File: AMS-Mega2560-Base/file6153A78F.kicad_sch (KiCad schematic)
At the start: 18 parts, among them Q17 BS250, Q21 LTV-847

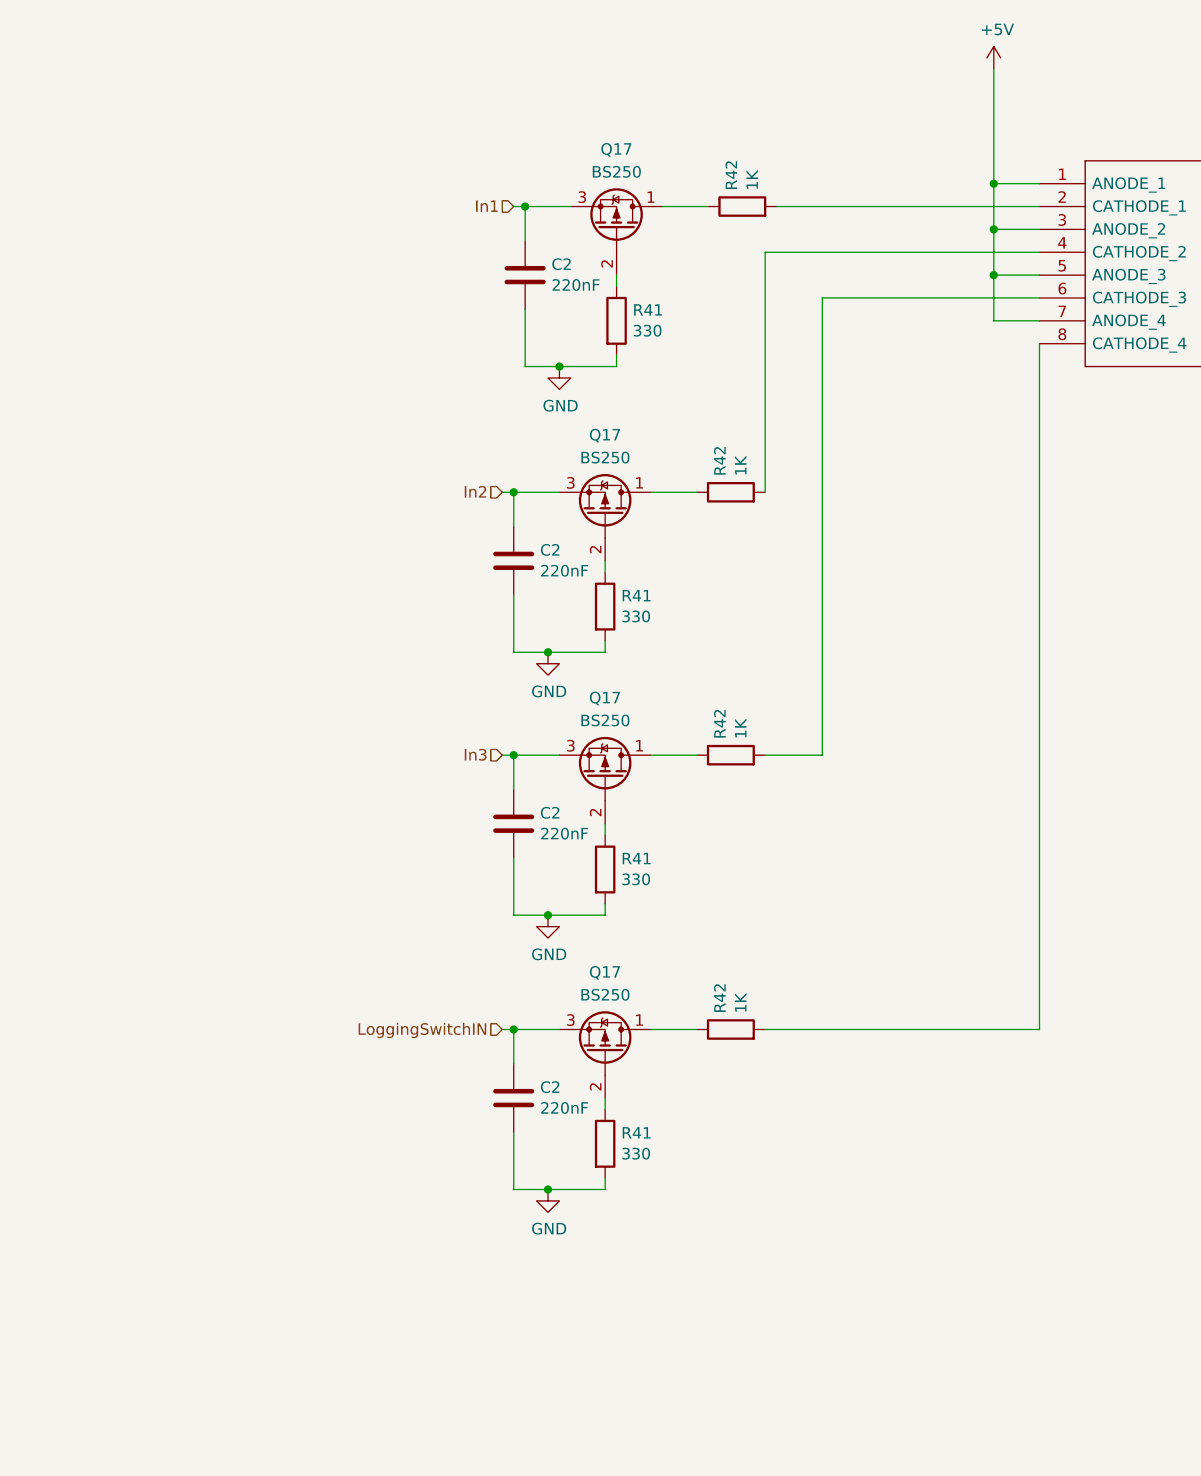
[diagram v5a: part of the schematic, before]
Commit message: * got parts placed * modified the Input circuit design to include Nchannel fet Needs the tricky routes done before doing autoroute
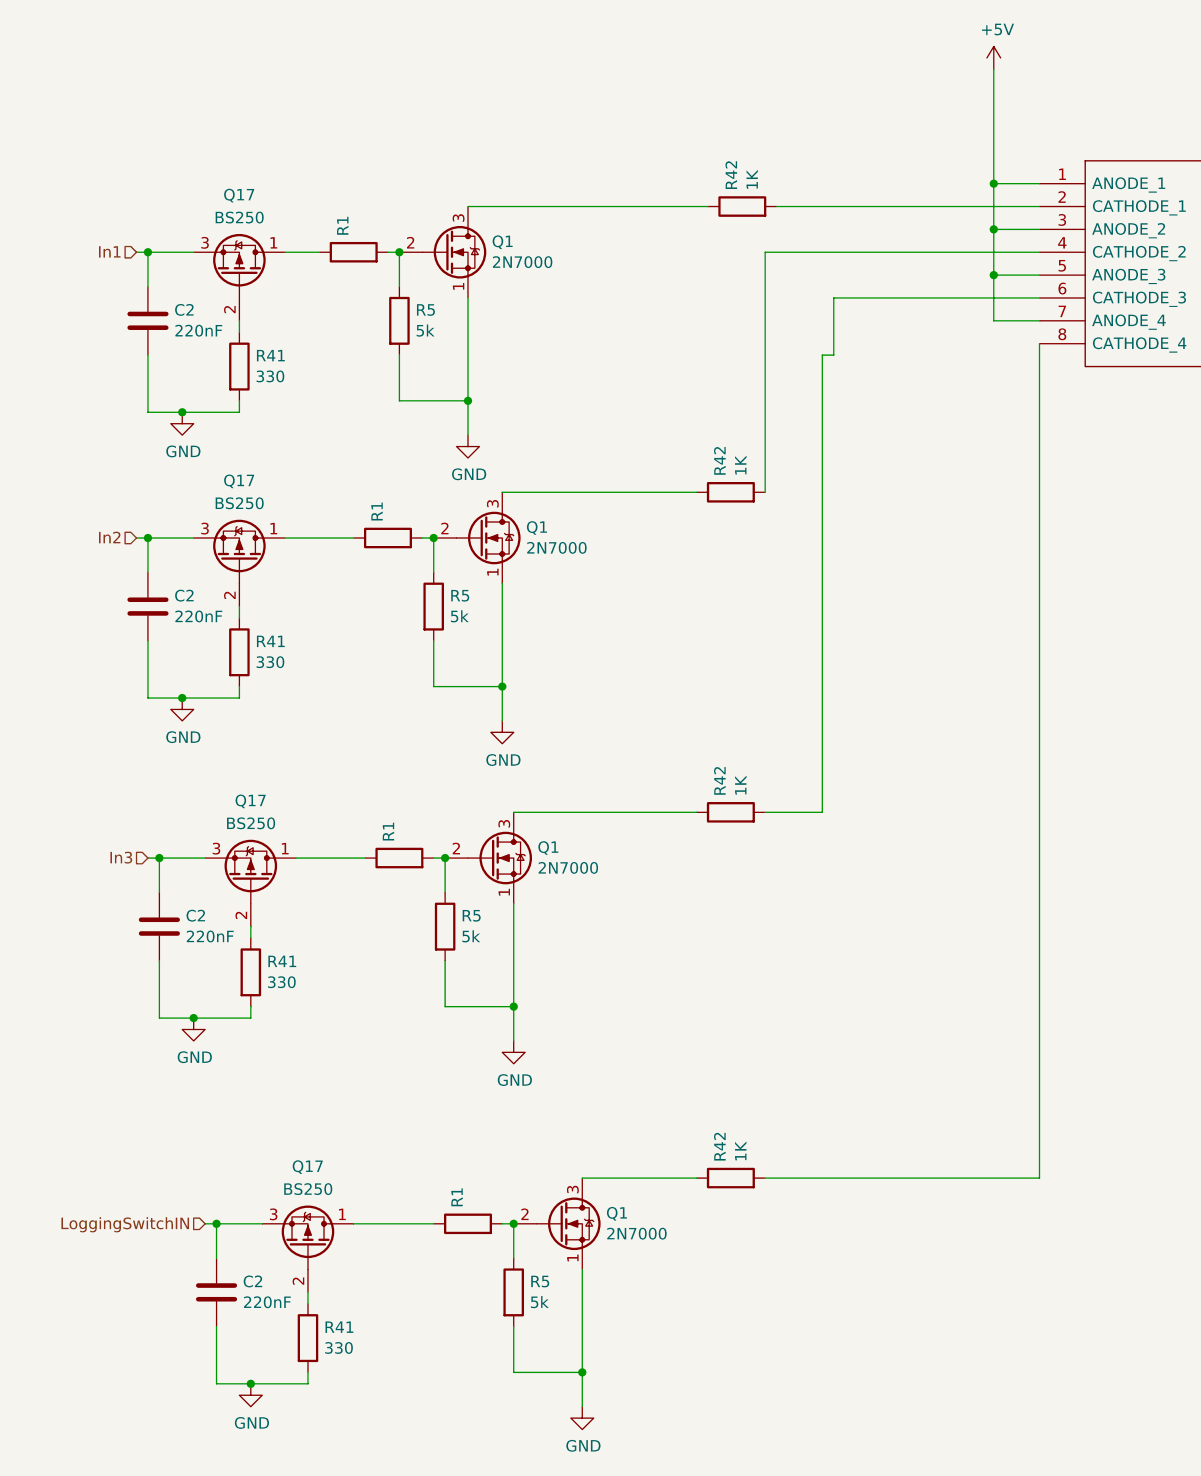
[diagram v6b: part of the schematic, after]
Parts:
- added Q1 (x4): 2N7000, Package_TO_SOT_THT:TO-92_Inline, symbol Transistor_FET:2N7000
- added R1 (x4): 470, Resistor_THT:R_Axial_DIN0207_L6.3mm_D2.5mm_P2.54mm_Vertical, symbol Device:R
- added R5 (x4): 5k, Resistor_THT:R_Axial_DIN0207_L6.3mm_D2.5mm_P2.54mm_Vertical, symbol Device:R
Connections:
- net GND: now also Q1.1 (S), Q1.1 (S), Q1.1 (S), Q1.1 (S), R5.2, R5.2, R5.2, R5.2
- net at R42.1: now also Q1.3 (D); no longer Q17.1 (D) (x2)
- net at Q17.1 (D): now also R1.1; no longer R42.1 (x2)
- new net: Q1.2 (G), R1.2, R5.1 (x4)
- new net: Q17.1 (D), R1.1 (x2)
- new net: Q1.3 (D), R42.1 (x2)
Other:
- moved on the sheet: C2, Q17, R41, R42
